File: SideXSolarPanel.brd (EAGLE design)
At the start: 81.7 x 102 mm, 33 parts

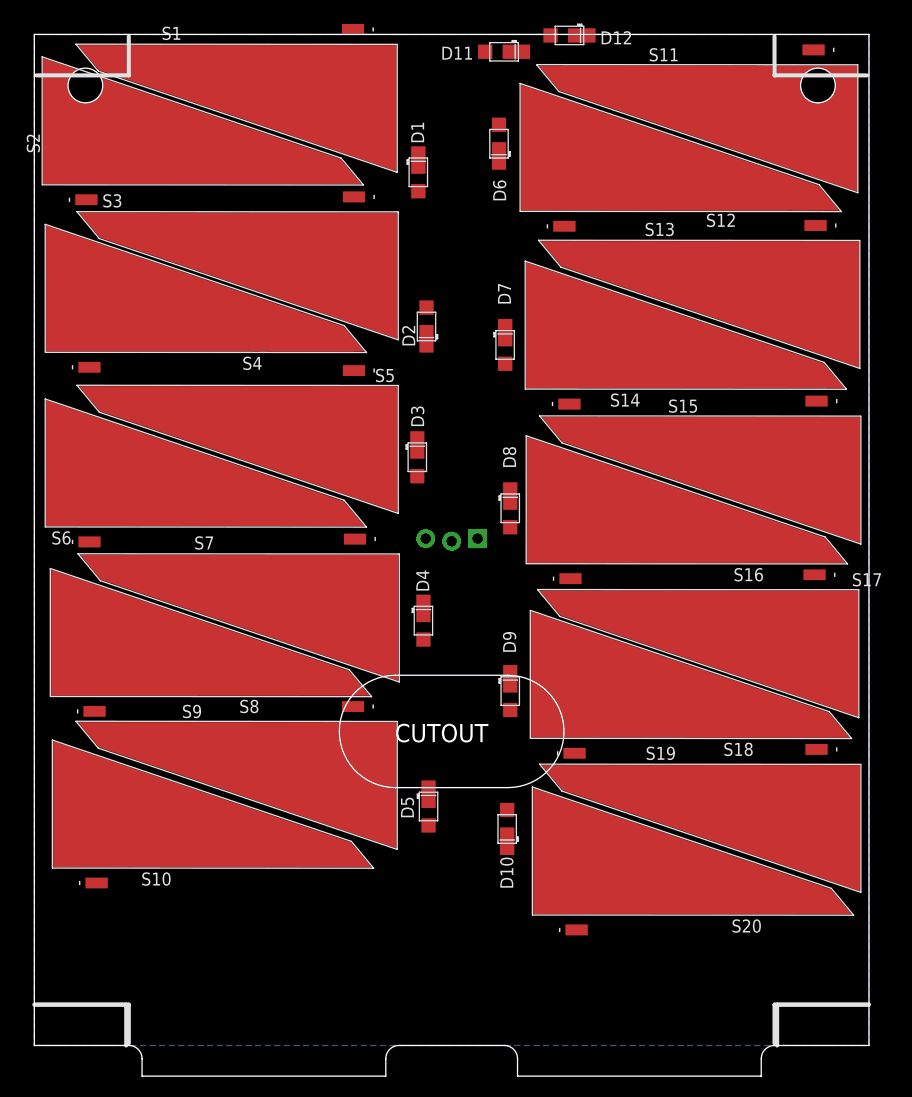
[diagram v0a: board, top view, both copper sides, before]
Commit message: Solar panel layout work
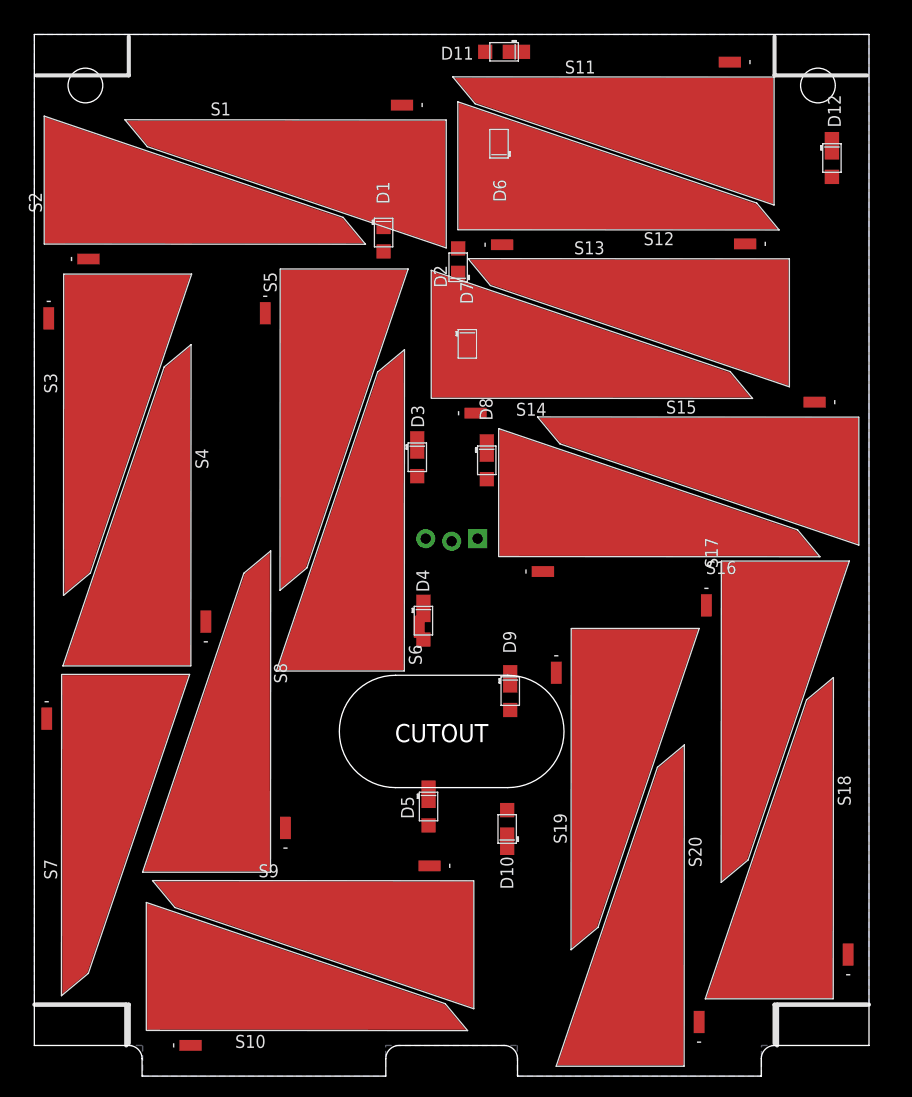
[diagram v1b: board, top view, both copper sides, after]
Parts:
- moved S7 31.9 mm to (2.80, 29.0), turned to 0 degrees
- moved S18 28.8 mm to (78.1, 11.9), turned to 180 degrees
- moved S3 28.6 mm to (3.00, 68.2), turned to 0 degrees
- moved S6 28.5 mm to (36.1, 44.0), turned to 180 degrees
- moved D12 28.4 mm to (78.1, 86.9), turned to 270 degrees
- moved S4 24.5 mm to (15.2, 44.5), turned to 180 degrees
- moved S19 21.8 mm to (52.7, 33.5), turned to 0 degrees
- moved S10 18.4 mm to (18.3, 1.60)
- moved S9 17.3 mm to (35.7, 16.0)
- moved S8 17.3 mm to (23.0, 24.3), turned to 180 degrees
- moved S20 10.6 mm to (63.5, 5.30), turned to 180 degrees
- moved S14 9.24 mm to (46.2, 63.5)
- moved S1 8.82 mm to (33.0, 90.5)
- moved S11 8.29 mm to (65.1, 94.7)
- moved S17 7.44 mm to (67.4, 40.1), turned to 0 degrees
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
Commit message: Finished routing X solar panel
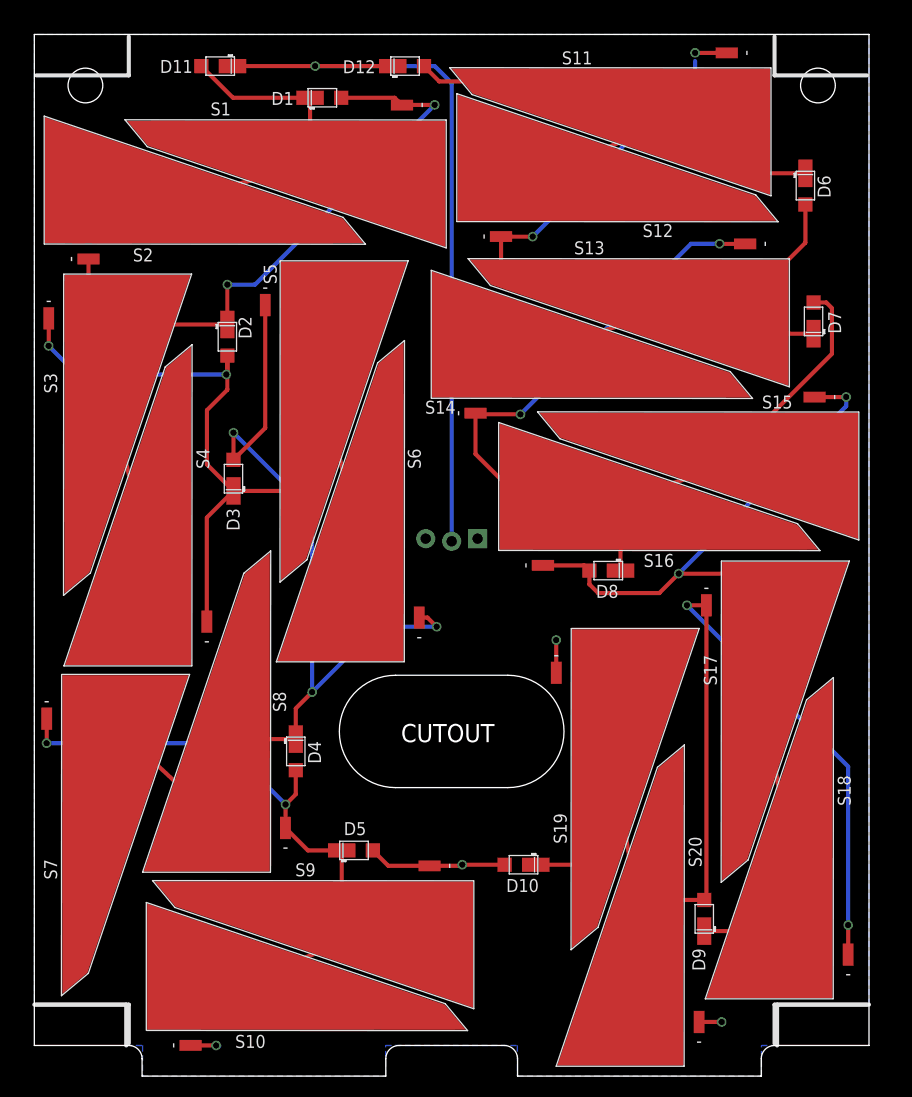
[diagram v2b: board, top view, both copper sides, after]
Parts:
- moved D12 42.8 mm to (36.3, 95.9), turned to 0 degrees
- moved D7 34.0 mm to (76.3, 70.9), turned to 90 degrees
- moved D6 30.3 mm to (75.5, 84.2), turned to 270 degrees
- moved D9 29.3 mm to (65.6, 12.4), turned to 90 degrees
- moved D11 27.8 mm to (18.2, 95.9)
- moved D2 23.6 mm to (18.9, 69.4), turned to 270 degrees
- moved D3 18.1 mm to (19.5, 55.5), turned to 90 degrees
- moved D4 17.9 mm to (25.6, 28.8)
- moved D8 16.1 mm to (56.2, 46.5), turned to 180 degrees
- moved D1 14.5 mm to (28.2, 92.8), turned to 0 degrees
- moved D5 8.47 mm to (31.3, 19.1), turned to 0 degrees
- moved D10 3.85 mm to (47.9, 17.7), turned to 180 degrees
- moved S11 0.95 mm to (64.8, 95.6)
- moved S6 0.90 mm to (36.1, 44.9)
- moved S12 0.81 mm to (48.7, 80.8)
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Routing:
- net N$41: track 0.00 -> 127.3 mm, vias 0 -> 2
- net N$7: track 0.00 -> 108.5 mm, vias 0 -> 2
- net N$39: track 0.00 -> 104.1 mm, vias 0 -> 3
- net N$37: track 0.00 -> 99.6 mm, vias 0 -> 2
- net N$36: track 0.00 -> 98.5 mm, vias 0 -> 2
- net N$1: track 0.00 -> 97.7 mm, vias 0 -> 2
- net N$45: track 0.00 -> 95.1 mm, vias 0 -> 2
- net N$50: track 0.00 -> 79.2 mm, vias 0 -> 2
- net N$5: track 0.00 -> 76.4 mm
- net V_SOLAR: track 0.00 -> 74.6 mm, vias 0 -> 1
- net N$9: track 0.00 -> 54.5 mm
- net GND: track 0.00 -> 22.5 mm, vias 0 -> 4

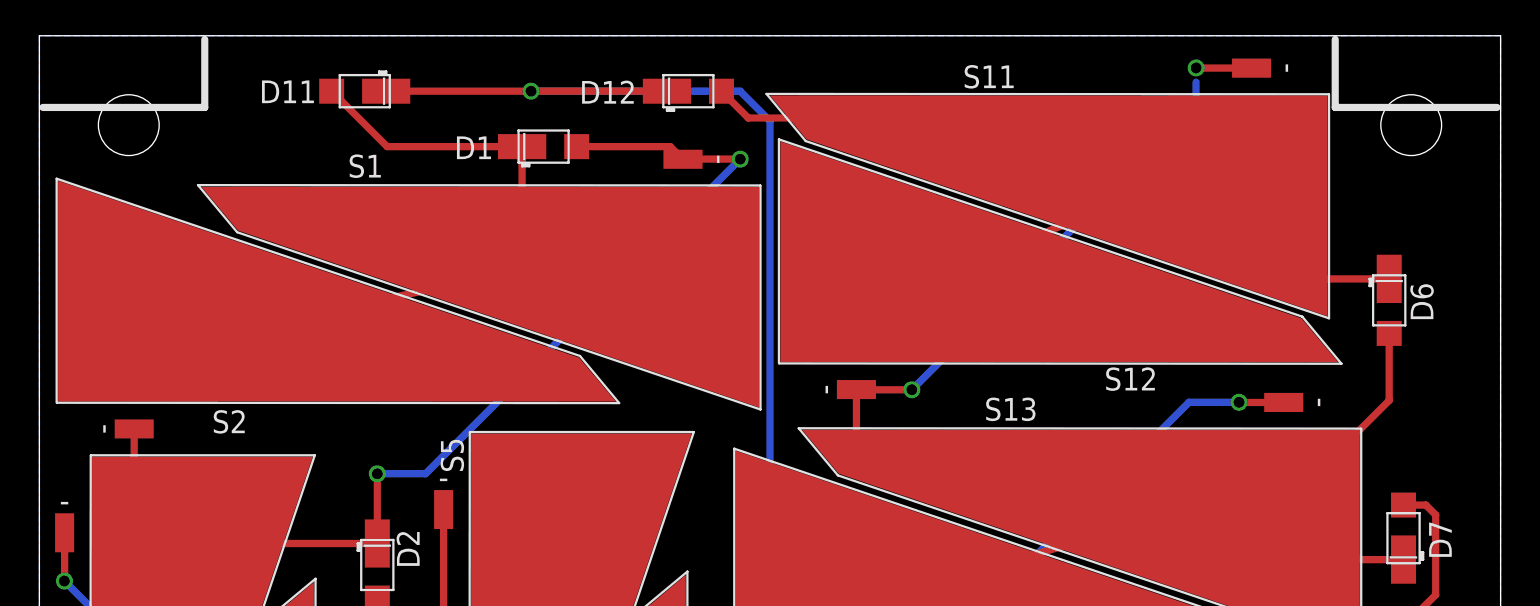
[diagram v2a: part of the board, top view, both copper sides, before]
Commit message: Moved screw holes on solar panel
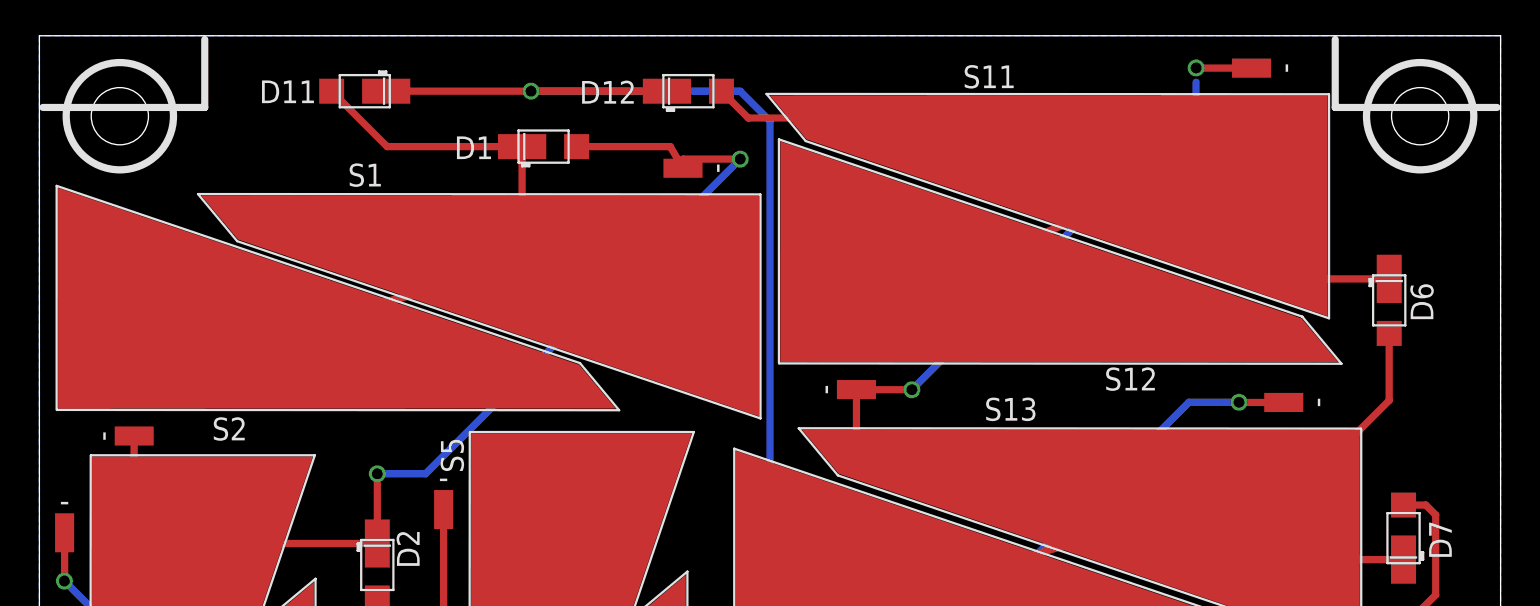
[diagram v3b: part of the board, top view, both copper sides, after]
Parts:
- moved S1 0.50 mm to (33.0, 90.0)
- moved S2 0.40 mm to (8.30, 78.2)
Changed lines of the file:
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@@
 <wire x1="72.48" y1="4" x2="72.48" y2="0.2" width="0.4" layer="121"/>
 <rectangle x1="13.1" y1="58.8" x2="28.9" y2="77.8" layer="122"/>
-<hole x="5" y="94" drill="3.4"/>
-<hole x="76.73" y="94" drill="3.4"/>
+<hole x="4.5" y="94.5" drill="3.2"/>
+<hole x="77.23" y="94.5" drill="3.2"/>
 <wire x1="35.365" y1="25.25" x2="46.365" y2="25.25" width="0" layer="20"/>
 <wire x1="35.365" y1="36.25" x2="46.365" y2="36.25" width="0" layer="20"/>
@@
 <wire x1="72.73" y1="4" x2="72.73" y2="0" width="0.4064" layer="21"/>
 <circle x="40.865" y="49.65" radius="7.5" width="0.254" layer="22"/>
+<circle x="4.5" y="94.5" radius="3" width="0.4064" layer="21"/>
+<circle x="77.23" y="94.5" radius="3" width="0.4064" layer="21"/>
 </plain>
 <attributes>
@@
 <attribute name="NAME" x="66.83" y="35.25" size="1.27" layer="25" rot="R90"/>
 </element>
-<element name="S2" library="phonesat" package="SOLAR_CELL" value="SOLAR_CELL" x="8.3" y="78.6" smashed="yes" rot="R90">
-<attribute name="NAME" x="9.65" y="76.77" size="1.27" layer="25"/>
+<element name="S2" library="phonesat" package="SOLAR_CELL" value="SOLAR_CELL" x="8.3" y="78.2" smashed="yes" rot="R90">
+<attribute name="NAME" x="9.65" y="76.37" size="1.27" layer="25"/>
 </element>
 <element name="S19" library="phonesat" package="SOLAR_CELL" value="SOLAR_CELL" x="52.7" y="33.5" smashed="yes">
@@
 <attribute name="NAME" x="64.07" y="20.45" size="1.27" layer="25" rot="R270"/>
 </element>
-<element name="S1" library="phonesat" package="SOLAR_CELL" value="SOLAR_CELL" x="33" y="90.5" smashed="yes" rot="R270">
-<attribute name="NAME" x="17.25" y="91.07" size="1.27" layer="25"/>
+<element name="S1" library="phonesat" package="SOLAR_CELL" value="SOLAR_CELL" x="33" y="90" smashed="yes" rot="R270">
+<attribute name="NAME" x="17.25" y="90.57" size="1.27" layer="25"/>
 </element>
 <element name="S15" library="phonesat" package="SOLAR_CELL" value="SOLAR_CELL" x="73.4" y="61.9" smashed="yes" rot="R270">
@@
 <contactref element="D11" pad="POS"/>
 <contactref element="S2" pad="2"/>
-<wire x1="38.0114" y1="88.3126" x2="27.800090625" y2="86.099584375" width="0.4064" layer="1"/>
-<wire x1="27.800090625" y1="86.099584375" x2="3.2886" y2="80.7874" width="0.4064" layer="1"/>
+<wire x1="38.0114" y1="87.8126" x2="27.800090625" y2="86.099584375" width="0.4064" layer="1"/>
+<wire x1="27.800090625" y1="86.099584375" x2="3.2886" y2="80.3874" width="0.4064" layer="1"/>
 <wire x1="27" y1="92.8" x2="27" y2="86.899675" width="0.4064" layer="1"/>
 <wire x1="27" y1="86.899675" x2="27.800090625" y2="86.099584375" width="0.4064" layer="1"/>
@@
 <wire x1="18.9" y1="70.6" x2="5.312421875" y2="70.6" width="0.4064" layer="1"/>
 <wire x1="5.312421875" y1="70.6" x2="5.312421875" y2="72.67941875" width="0.4064" layer="1"/>
-<wire x1="5.3009" y1="77.0107" x2="5.3009" y2="73.3249" width="0.4064" layer="1"/>
+<wire x1="5.3009" y1="76.6107" x2="5.3009" y2="73.3249" width="0.4064" layer="1"/>
 <wire x1="5.3009" y1="73.3249" x2="5.1874" y2="73.2114" width="0.4064" layer="1"/>
 <wire x1="30.05" y1="92.8" x2="35.2884" y2="92.8" width="0.4064" layer="1"/>
-<wire x1="35.2884" y1="92.8" x2="35.9991" y2="92.0893" width="0.4064" layer="1"/>
+<wire x1="35.2884" y1="92.8" x2="35.9991" y2="91.5893" width="0.4064" layer="1"/>
 <wire x1="18.9" y1="70.6" x2="18.9" y2="74.5" width="0.4064" layer="1"/>
 <via x="18.9" y="74.5" extent="1-16" drill="0.6"/>
@@
 <via x="39.2" y="92.1" extent="1-16" drill="0.6"/>
 <wire x1="39.2" y1="92.1" x2="36.0098" y2="92.1" width="0.4064" layer="1"/>
-<wire x1="36.0098" y1="92.1" x2="35.9991" y2="92.0893" width="0.4064" layer="1"/>
+<wire x1="36.0098" y1="92.1" x2="35.9991" y2="91.5893" width="0.4064" layer="1"/>
 </signal>
 <signal name="N$50">

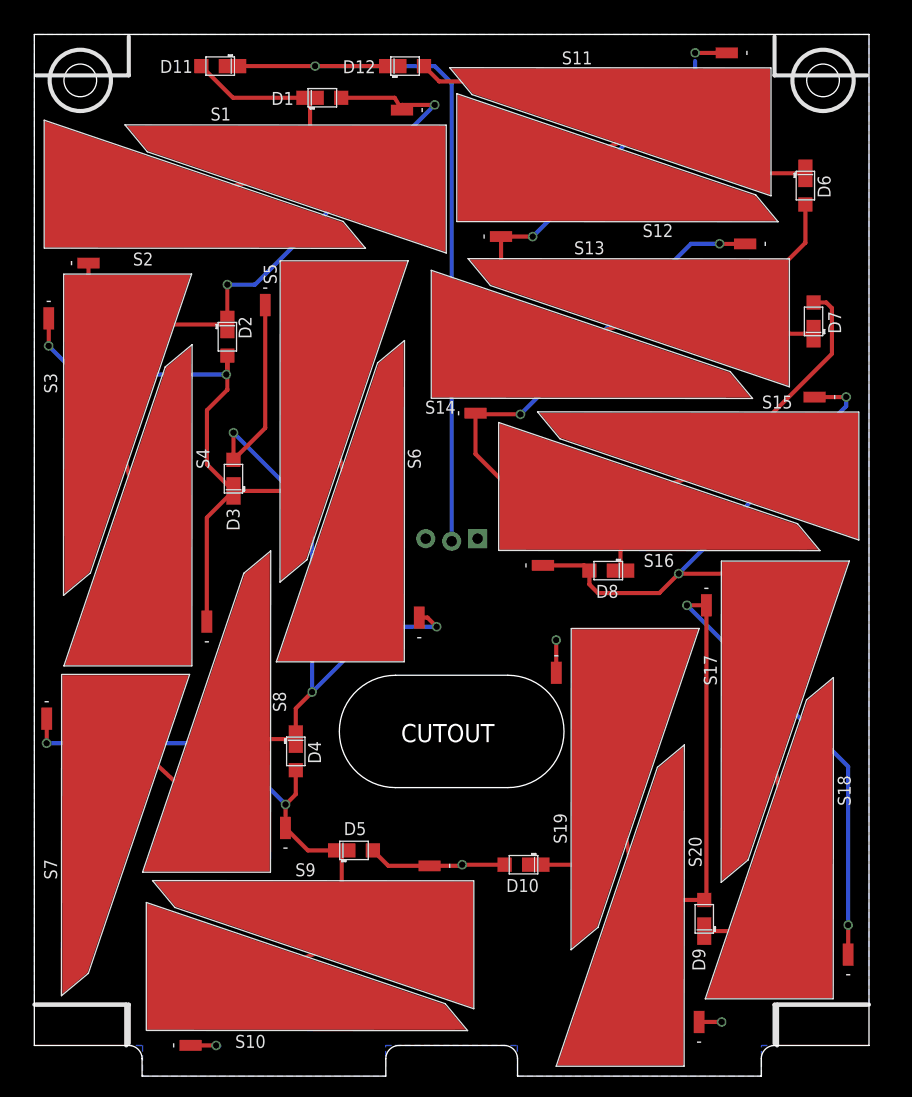
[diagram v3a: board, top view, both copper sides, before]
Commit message: Finished routing Y solar panel
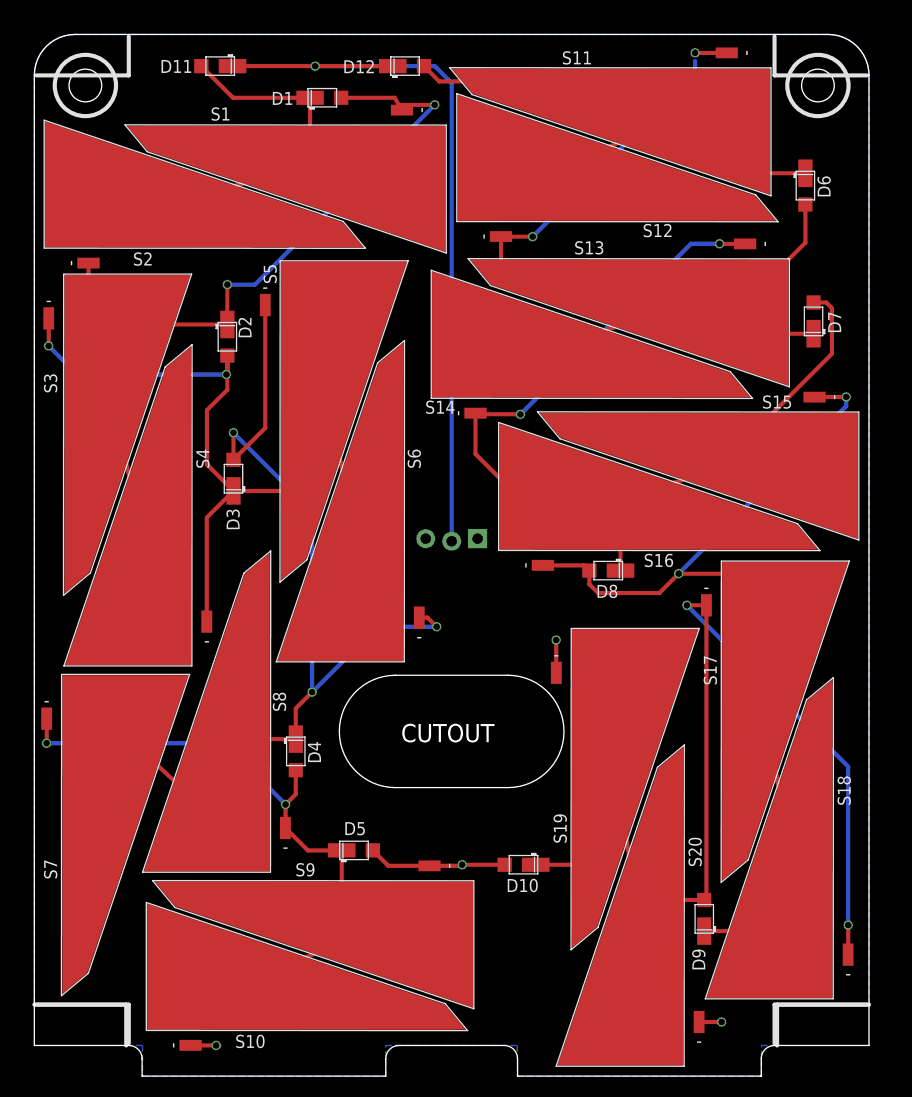
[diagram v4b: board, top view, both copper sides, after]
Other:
- outline, holes or cut-outs redrawn
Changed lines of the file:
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@@
 <board>
 <plain>
-<wire x1="81.73" y1="99" x2="81.73" y2="0" width="0" layer="20"/>
-<wire x1="0" y1="99" x2="0" y2="0" width="0" layer="20"/>
+<wire x1="81.73" y1="0" x2="81.73" y2="95" width="0" layer="20"/>
+<wire x1="81.73" y1="95" x2="77.73" y2="99" width="0" layer="20" curve="90"/>
+<wire x1="77.73" y1="99" x2="4" y2="99" width="0" layer="20"/>
+<wire x1="4" y1="99" x2="0" y2="95" width="0" layer="20" curve="90"/>
+<wire x1="0" y1="95" x2="0" y2="0" width="0" layer="20"/>
 <wire x1="0" y1="0" x2="9.25" y2="0" width="0" layer="20"/>
 <wire x1="10.55" y1="-1.3" x2="10.55" y2="-3" width="0" layer="20"/>
@@
 <wire x1="46.015" y1="0" x2="47.315" y2="-1.3" width="0" layer="20" curve="-90"/>
 <wire x1="71.18" y1="-1.3" x2="72.48" y2="0" width="0" layer="20" curve="-90"/>
-<wire x1="81.73" y1="99" x2="0" y2="99" width="0" layer="20"/>
 <wire x1="0.2" y1="4" x2="9.25" y2="4" width="0.4" layer="121"/>
 <wire x1="9.25" y1="4" x2="9.25" y2="0.2" width="0.4" layer="121"/>
@@
 <wire x1="72.48" y1="4" x2="72.48" y2="0.2" width="0.4" layer="121"/>
 <rectangle x1="13.1" y1="58.8" x2="28.9" y2="77.8" layer="122"/>
-<hole x="4.5" y="94.5" drill="3.2"/>
-<hole x="77.23" y="94.5" drill="3.2"/>
+<hole x="5" y="94" drill="3.2"/>
+<hole x="76.73" y="94" drill="3.2"/>
 <wire x1="35.365" y1="25.25" x2="46.365" y2="25.25" width="0" layer="20"/>
 <wire x1="35.365" y1="36.25" x2="46.365" y2="36.25" width="0" layer="20"/>
@@
 <wire x1="72.73" y1="4" x2="72.73" y2="0" width="0.4064" layer="21"/>
 <circle x="40.865" y="49.65" radius="7.5" width="0.254" layer="22"/>
-<circle x="4.5" y="94.5" radius="3" width="0.4064" layer="21"/>
-<circle x="77.23" y="94.5" radius="3" width="0.4064" layer="21"/>
+<circle x="5" y="94" radius="3" width="0.4064" layer="21"/>
+<circle x="76.73" y="94" radius="3" width="0.4064" layer="21"/>
 </plain>
 <attributes>
@@
 <contactref element="D10" pad="POS"/>
 <polygon width="0.2" layer="16" thermals="no">
-<vertex x="81.73" y="99"/>
-<vertex x="0" y="99"/>
+<vertex x="81.73" y="4"/>
+<vertex x="81.73" y="95" curve="90"/>
+<vertex x="77.73" y="99"/>
+<vertex x="4" y="99" curve="90"/>
+<vertex x="0" y="95"/>
 <vertex x="0" y="4"/>
 <vertex x="9" y="4"/>
@@
 <vertex x="72.73" y="0"/>
 <vertex x="72.73" y="4"/>
-<vertex x="81.73" y="4"/>
 </polygon>
 <contactref element="S9" pad="1"/>
